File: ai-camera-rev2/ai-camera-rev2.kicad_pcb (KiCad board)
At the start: 4 copper layers, 70 x 70 mm, 178 parts, among them J1 Conn-01x02_P2mm_NONAME_JST-PH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, J2 TYPE-C-31-M-12, J3 MAXLAB, J4 Conn-02x10_P2.54mm_B-2100S20P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, J5 Conn-01x02_P1.25mm_10114829-1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, J6 Conn_01x24_FFC_0.5mm_AFC01-S2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, Q1 2N7002, Q10 2N7002, Q2 2N7002, Q3 AO3401A, Q4 AO3401A, Q5 2N7002, Q6 AO3401A, Q7 2N7002, Q8 AO3401A, Q9 2N7002, SW1 SW_PB_90deg_K2-1102AQ-H4CW-01, SW2 SW_PB_TS-1187A-B-A-B, SW3 SW_PB_TS-1187A-B-A-B, SW4 SW_PB_90deg_K2-1102AQ-H4CW-01, U1 TP4057-42-SOT26-R, U10 ESP32-S3-WROOM-1-N16R8, U11 MT9284-28J, U12 LTR-303ALS-01, U2 XC6206-2.8V, U3 PCF85063AT_SO8, U4 SOT-23-6_SN74LVC1G373DBVR_TI, U5 SY8089AAAC, U6 PIR_AS312, U7 XC6206-2.8V, U8 RT9166-12GVL, U9 AP1511B, Y1 32.768kHz_Q13FC1350000400

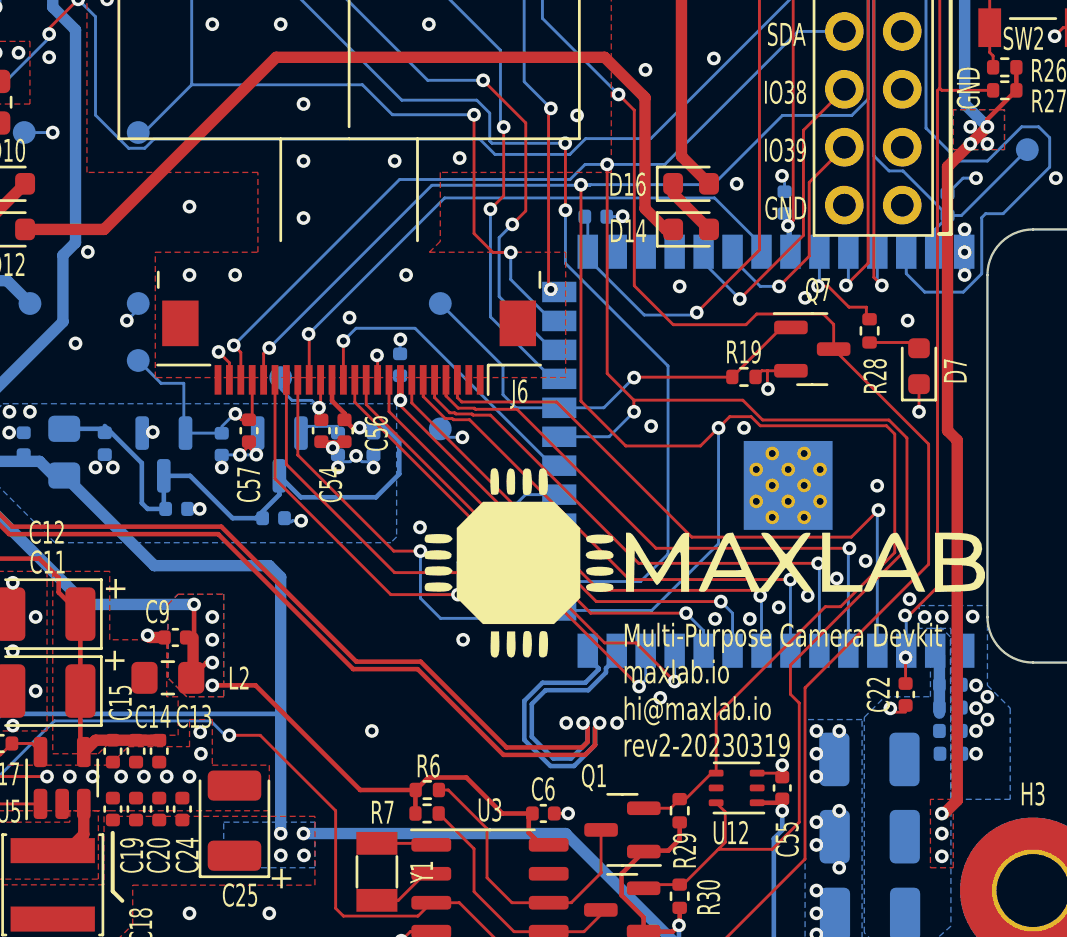
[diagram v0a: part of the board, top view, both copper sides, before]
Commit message: EAC-49: move camera connector to avoid FPC cable bending
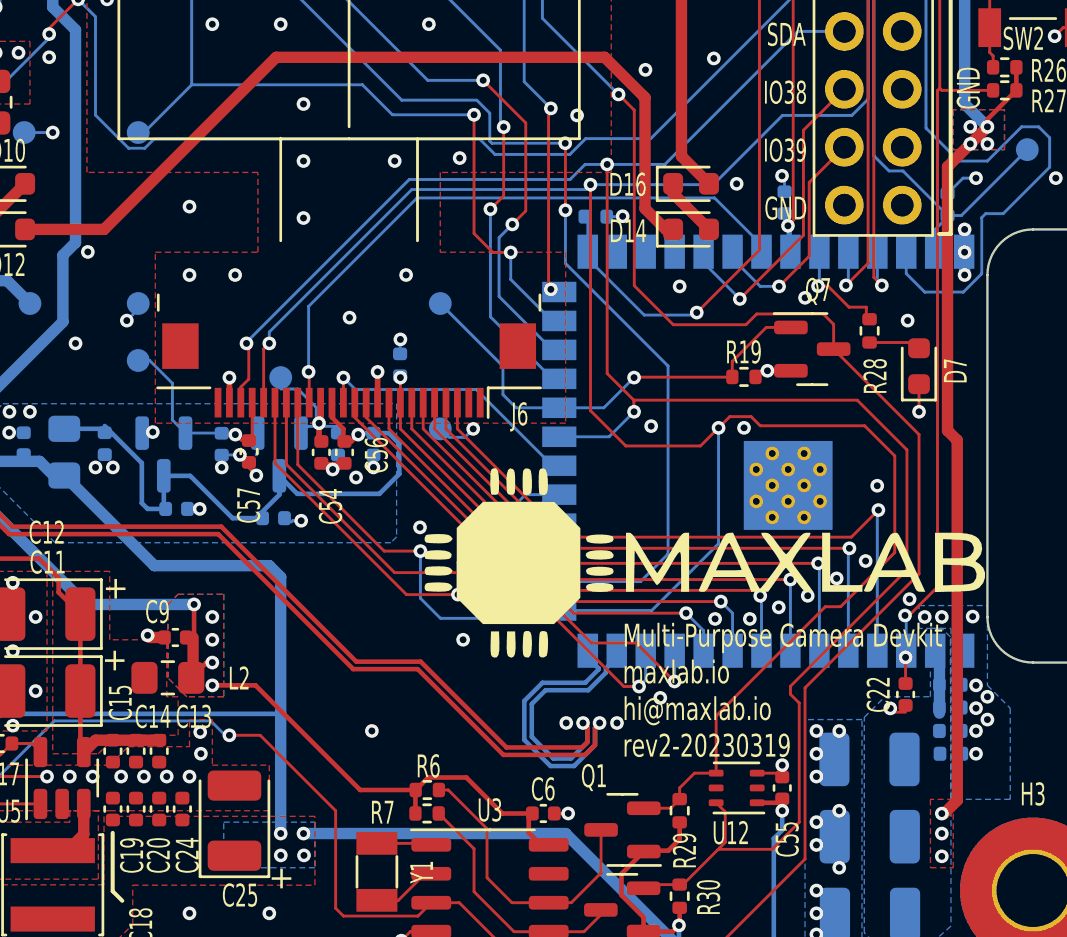
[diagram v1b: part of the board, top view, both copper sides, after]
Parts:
- moved J6 1.00 mm to (130.0, 87.0)
- moved C54 0.95 mm to (128.8, 90.8)
- moved C56 0.95 mm to (129.8, 90.8)
- moved C57 0.91 mm to (125.6, 90.7)
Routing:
- net GND: track 93.0 -> 88.2 mm, vias 203 -> 202
- net /CAM.D9: track 13.6 -> 11.9 mm
- net /CAM.HREF: track 25.2 -> 26.9 mm
- net /CAM.RST: track 21.6 -> 20.2 mm
- net +1V2: track 6.35 -> 5.17 mm
- net +2V8: track 8.97 -> 7.96 mm
- net /CAM.VSYNC: track 18.5 -> 17.5 mm
- net /PWR_EN: track 19.1 -> 19.9 mm
- net /CAM.PWDN: track 20.8 -> 20.0 mm
- net /CAM.D6: track 21.6 -> 22.3 mm
- net /CAM.D8: track 21.0 -> 20.3 mm
- net /CAM.MCLK: track 20.3 -> 19.7 mm
- net /CAM.D7: track 20.0 -> 19.5 mm
- net /CAM.SCL: track 99.0 -> 99.5 mm
